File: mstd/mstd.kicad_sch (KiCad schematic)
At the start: 19 parts, among them SW1 TSX101G100-250, U1 ICE40UP5K-SG48ITR, U5 74LVX3245MTCX, U6 74LVX3245MTCX, U7 SSD1306 OLED

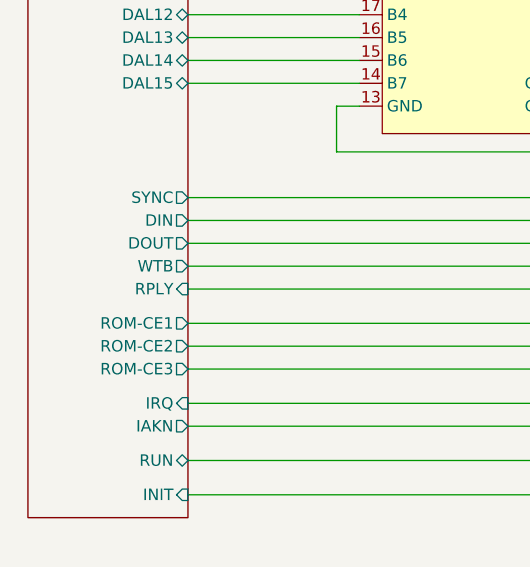
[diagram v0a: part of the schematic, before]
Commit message: FPGA pins swapped for bring SYNC to G* pin
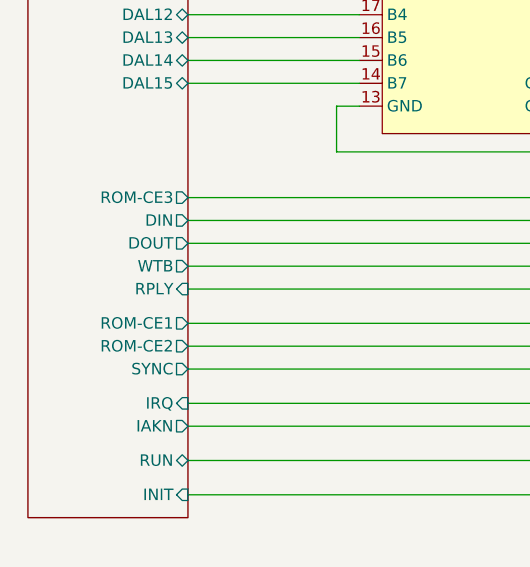
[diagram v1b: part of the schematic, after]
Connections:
- net IO/ROM-CE3: now also U1.23 (IOT_37a); no longer U1.37 (IOT_45a_G1)
- net IO/SYNC: now also U1.37 (IOT_45a_G1); no longer U1.23 (IOT_37a)
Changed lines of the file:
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@@
 	(wire
 		(pts
-			(xy 69.85 121.92) (xy 177.8 121.92)
-		)
-		(stroke
-			(width 0)
-			(type default)
-		)
-	)
-	(wire
-		(pts
 			(xy 187.96 102.87) (xy 191.77 102.87)
 		)
@@
 	(wire
 		(pts
-			(xy 69.85 140.97) (xy 142.24 140.97)
-		)
-		(stroke
-			(width 0)
-			(type default)
-		)
-	)
-	(wire
-		(pts
 			(xy 130.81 119.38) (xy 177.8 119.38)
 		)
@@
 	(wire
 		(pts
+			(xy 69.85 121.92) (xy 177.8 121.92)
+		)
+		(stroke
+			(width 0)
+			(type default)
+		)
+	)
+	(wire
+		(pts
 			(xy 144.78 142.24) (xy 177.8 142.24)
 		)
@@
 	(wire
 		(pts
+			(xy 69.85 140.97) (xy 142.24 140.97)
+		)
+		(stroke
+			(width 0)
+			(type default)
+		)
+	)
+	(wire
+		(pts
 			(xy 137.16 135.89) (xy 137.16 134.62)
 		)
@@
 		)
 		(pin "SYNC" output
-			(at 69.85 121.92 0)
+			(at 69.85 140.97 0)
 			(effects
 				(font
@@
 		)
 		(pin "ROM-CE3" output
-			(at 69.85 140.97 0)
+			(at 69.85 121.92 0)
 			(effects
 				(font

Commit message: Routing started
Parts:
- added C15: 1.0, Capacitor_SMD:C_0603_1608Metric_Pad1.08x0.95mm_HandSolder, symbol Device:C
- added TP1, TP2, TP3, TP4: TestPoint, TestPoint:TestPoint_THTPad_D1.0mm_Drill0.5mm, symbol Connector:TestPoint
- C14, C19, C24, C25, C26, C27: footprint (none) -> Capacitor_SMD:C_0603_1608Metric_Pad1.08x0.95mm_HandSolder
- R3, R32, R4, R5, R6, R7, R8, R9: footprint (none) -> Resistor_SMD:R_0603_1608Metric_Pad0.98x0.95mm_HandSolder
- U7: footprint local1:SDD1306 -> local:SDD1306
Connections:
- net +3V3: now also C15.1
- net GND: now also C15.2
- net at U1.39 (RGB0): now also TP2.1
- net at U1.40 (RGB1): now also TP3.1
- net at U1.41 (RGB2): now also TP4.1
- net at U1.42 (IOT_51a): now also TP1.1
- no-connect marks 6 -> 2

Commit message: Routhing in finilizing stage
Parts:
- added H1, H2, H3, H4: MountingHole, MountingHole:MountingHole_3.2mm_M3_ISO14580, symbol Mechanical:MountingHole
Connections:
- net IO/ROM-CE3 is gone; now on net IO/INIT: U1.23 (IOT_37a)
- net IO/RUN is gone; now on net A12: U1.43 (IOT_49a)
- net IO/WTB is gone; now on net IO/IRQ: U1.28 (IOT_41a)
- net CPU/CI2: now also R5.1, SW1.4; no longer R7.1, SW1.6
- net CPU/CIO0: now also R7.1, SW1.6; no longer R5.1, SW1.4
- net CPU/FIO0: now also U5.6 (A3); no longer U5.3 (A0)
- net CPU/FIO1: now also U5.5 (A2); no longer U5.4 (A1)
- net CPU/FIO2: now also U5.4 (A1); no longer U5.5 (A2)
- net CPU/FIO3: now also U5.3 (A0); no longer U5.6 (A3)
- net CPU/FIO4: now also R32.1, U5.2 (T/~{R}), U6.2 (T/~{R}); no longer U5.7 (A4)
- net IO/DIN: now also U1.34 (IOT_44b); no longer U1.27 (IOT_38b)
- net IO/DOUT: now also U1.32 (IOT_43a); no longer U1.26 (IOT_39a)
- net IO/IAKN: now also U1.35 (IOT_46b_G0); no longer U1.36 (IOT_48b)
- net IO/INIT: no longer U1.38 (IOT_50b)
- net IO/IRQ: no longer U1.35 (IOT_46b_G0)
- net IO/ROM-CE1: now also U1.27 (IOT_38b); no longer U1.32 (IOT_43a)
- net IO/ROM-CE2: now also U1.26 (IOT_39a); no longer U1.34 (IOT_44b)
- net A15: now reaches U6.10 (A7)
- net A15: now also U1.36 (IOT_48b); no longer U1.3 (IOB_9b)
- net at U6.3 (A0): now also U1.47 (IOB_2a); no longer U1.46 (IOB_0a)
- net at U6.4 (A1): now also U1.46 (IOB_0a); no longer U1.47 (IOB_2a)
- net at U6.5 (A2): now also U1.45 (IOB_5b); no longer U1.44 (IOB_3b_G6)
- net at U6.6 (A3): now also U1.44 (IOB_3b_G6); no longer U1.48 (IOB_4a)
- net A12: now reaches U6.7 (A4)
- net A12: no longer U1.45 (IOB_5b)
- net A13: now reaches U6.8 (A5)
- net A13: now also U1.42 (IOT_51a); no longer U1.2 (IOB_6a)
- net A14: now reaches U6.9 (A6)
- net A14: now also U1.38 (IOT_50b); no longer U1.4 (IOB_8a)
- net at TP1.1: now also U1.25 (IOT_36b); no longer U1.42 (IOT_51a)
- net CPU/CIO6 renamed CPU/CIO1
- net CPU/CIO7 renamed CPU/CIO2
- net CPU/FIO5 renamed A5
- net A5: now also U1.3 (IOB_9b)
- net CPU/FIO6 renamed A6
- net A6: now also U1.2 (IOB_6a)
- net CPU/FIO7 renamed A7
- net A7: now also U1.48 (IOB_4a)
- new net A4: U1.4 (IOB_8a), U5.7 (A4)

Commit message: Fixes 74LVCX3245 package
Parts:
- U5, U6: footprint easyeda2kicad:TSSOP-24_L7.8-W4.4-P0.65-LS6.4-BL -> Package_SO:SOP-24_7.5x15.4mm_P1.27mm
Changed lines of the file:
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@@
 			)
 		)
-		(property "Footprint" "easyeda2kicad:TSSOP-24_L7.8-W4.4-P0.65-LS6.4-BL"
+		(property "Footprint" "Package_SO:SOP-24_7.5x15.4mm_P1.27mm"
 			(at 101.6 71.12 0)
 			(effects
@@
 			)
 		)
-		(property "Footprint" "easyeda2kicad:TSSOP-24_L7.8-W4.4-P0.65-LS6.4-BL"
+		(property "Footprint" "Package_SO:SOP-24_7.5x15.4mm_P1.27mm"
 			(at 101.6 119.38 0)
 			(effects

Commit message: Finalized PCB
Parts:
- added JP1, JP2: SolderJumper_3_Bridged12, Jumper:SolderJumper-3_P1.3mm_Bridged12_RoundedPad1.0x1.5mm, symbol Jumper:SolderJumper_3_Bridged12
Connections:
- net +3V3: now also JP1.1 (A), JP2.3 (B); no longer C15.1, U7.1 (VCC)
- net GND: now also JP1.3 (B), JP2.1 (A); no longer C15.2, U7.2 (GND)
- new net: C15.1, JP2.2 (C), U7.1 (GND)
- new net: C15.2, JP1.2 (C), U7.2 (VCC)
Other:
- moved on the sheet: C15, U7
